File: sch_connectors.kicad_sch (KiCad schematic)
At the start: 14 parts, among them J1 Conn_02x10_Odd_Even, J2 Conn_01x10

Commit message: Added two 1x2 12V power connectors and 4x bypassing caps
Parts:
- added C81, C82, C83, C84: 10UF 25V, $Local:C_0805_2012Metric, symbol $Local:C_0805_10UF_25V
- added J3, J4: Conn_01x02, $Local:PinHeader_1x02_P2.54mm_Vertical, symbol $Local:Conn_01x02
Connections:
- net +12V: now also C81.1, C82.1, C83.1, C84.1, J3.1 (Pin_1), J4.1 (Pin_1)
- net GND: now also C81.2, C82.2, C83.2, C84.2, J3.2 (Pin_2), J4.2 (Pin_2)

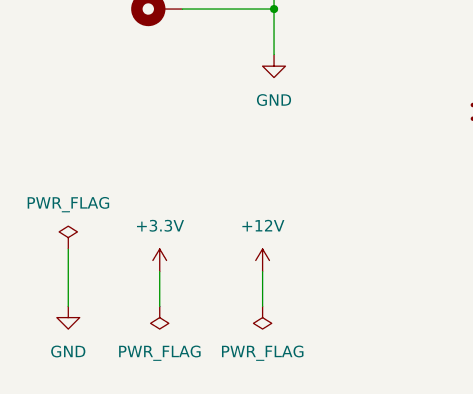
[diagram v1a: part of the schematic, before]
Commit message: Added pull-downs to output of Sense filter op amps
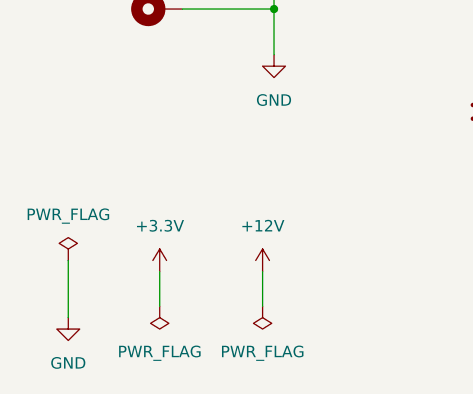
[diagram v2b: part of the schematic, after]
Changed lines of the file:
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@@
 	(wire
 		(pts
-			(xy 29.21 171.45) (xy 29.21 177.8)
+			(xy 29.21 172.72) (xy 29.21 179.07)
 		)
 		(stroke
@@
 	(symbol
 		(lib_id "$Local:GND")
-		(at 29.21 177.8 0)
+		(at 29.21 179.07 0)
 		(unit 1)
 		(exclude_from_sim no)
@@
 		(fields_autoplaced yes)
 		(property "Reference" "#PWR08"
-			(at 29.21 184.15 0)
+			(at 29.21 185.42 0)
 			(effects
 				(font
@@
 		)
 		(property "Value" "GND"
-			(at 29.21 182.88 0)
+			(at 29.21 184.15 0)
 			(effects
 				(font
@@
 		)
 		(property "Footprint" ""
-			(at 29.21 177.8 0)
+			(at 29.21 179.07 0)
 			(effects
 				(font
@@
 		)
 		(property "Datasheet" ""
-			(at 29.21 177.8 0)
+			(at 29.21 179.07 0)
 			(effects
 				(font
@@
 		)
 		(property "Description" "Power symbol creates a global label with name \"GND\" , ground"
-			(at 29.21 177.8 0)
+			(at 29.21 179.07 0)
 			(effects
 				(font
@@
 	(symbol
 		(lib_id "power:PWR_FLAG")
-		(at 29.21 171.45 0)
+		(at 29.21 172.72 0)
 		(unit 1)
 		(exclude_from_sim no)
@@
 		(fields_autoplaced yes)
 		(property "Reference" "#FLG01"
-			(at 29.21 169.545 0)
+			(at 29.21 170.815 0)
 			(effects
 				(font
@@
 		)
 		(property "Value" "PWR_FLAG"
-			(at 29.21 166.37 0)
+			(at 29.21 167.64 0)
 			(effects
 				(font
@@
 		)
 		(property "Footprint" ""
-			(at 29.21 171.45 0)
+			(at 29.21 172.72 0)
 			(effects
 				(font
@@
 		)
 		(property "Datasheet" "~"
-			(at 29.21 171.45 0)
+			(at 29.21 172.72 0)
 			(effects
 				(font
@@
 		)
 		(property "Description" "Special symbol for telling ERC where power comes from"
-			(at 29.21 171.45 0)
+			(at 29.21 172.72 0)
 			(effects
 				(font
